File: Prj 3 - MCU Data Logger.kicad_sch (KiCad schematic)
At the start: 25 parts, among them U1 24LC1025, U2 24LC1025, U3 DS1337S_, U4 ATMEGA328P-AU, Y1 Crystal, Y2 Crystal

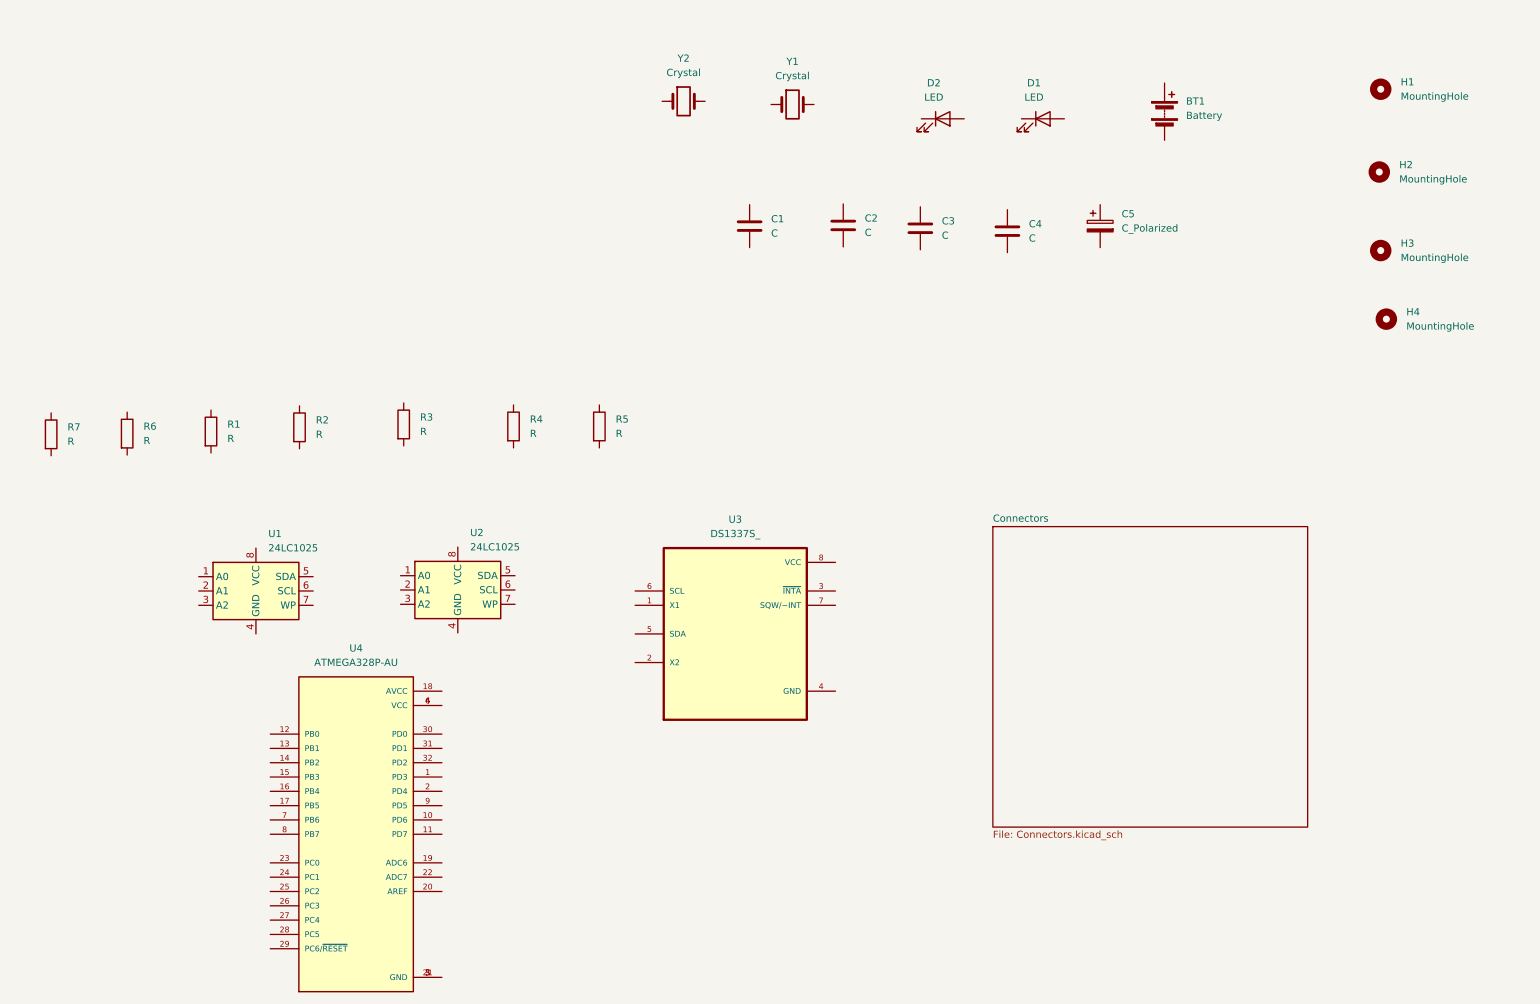
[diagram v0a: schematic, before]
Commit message: Placed symbols and added component values
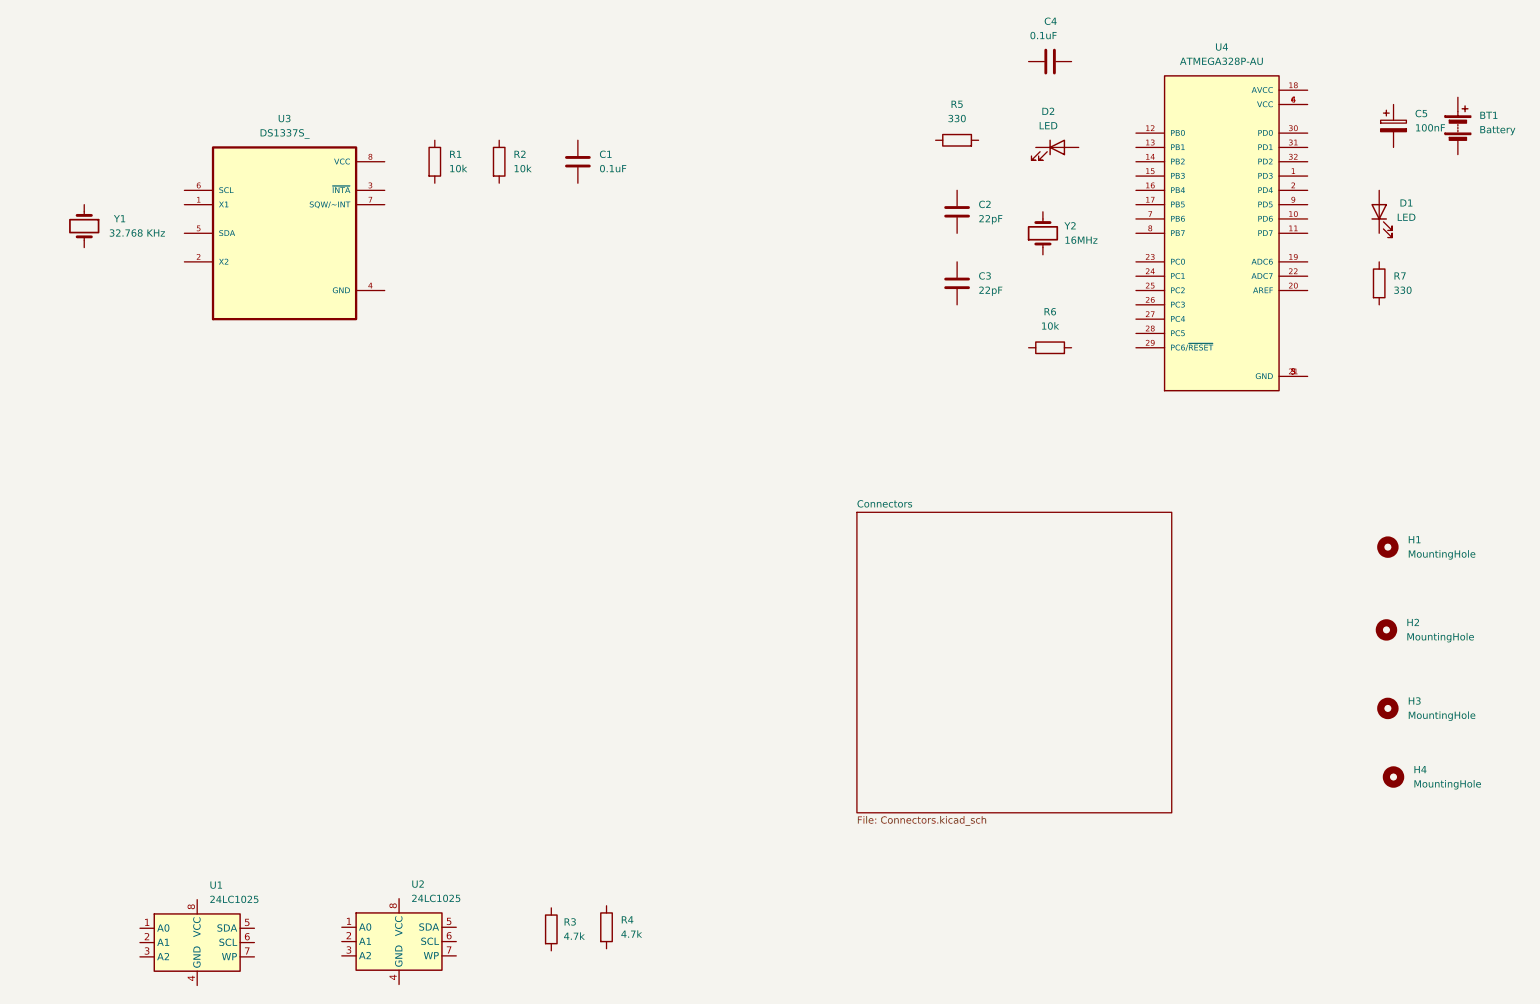
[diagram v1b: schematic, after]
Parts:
- C1, C4: value C -> 0.1uF
- C2: renamed from C3; value C -> 22pF
- C3: renamed from C2; value C -> 22pF
- C5: value C_Polarized -> 100nF
- R1: renamed from R2; value R -> 10k
- R2: renamed from R3; value R -> 10k
- R3: renamed from R6; value R -> 4.7k
- R4: renamed from R1; value R -> 4.7k
- R5: renamed from R4; value R -> 330
- R6: renamed from R7; value R -> 10k
- R7: renamed from R5; value R -> 330
- Y1: renamed from Y2; value Crystal -> 32.768 KHz
- Y2: renamed from Y1; value Crystal -> 16MHz
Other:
- moved on the sheet: BT1, C1, C2, C3, C4, C5, D1, D2, H1, H2, H3, H4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

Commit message: add footprints to symbols
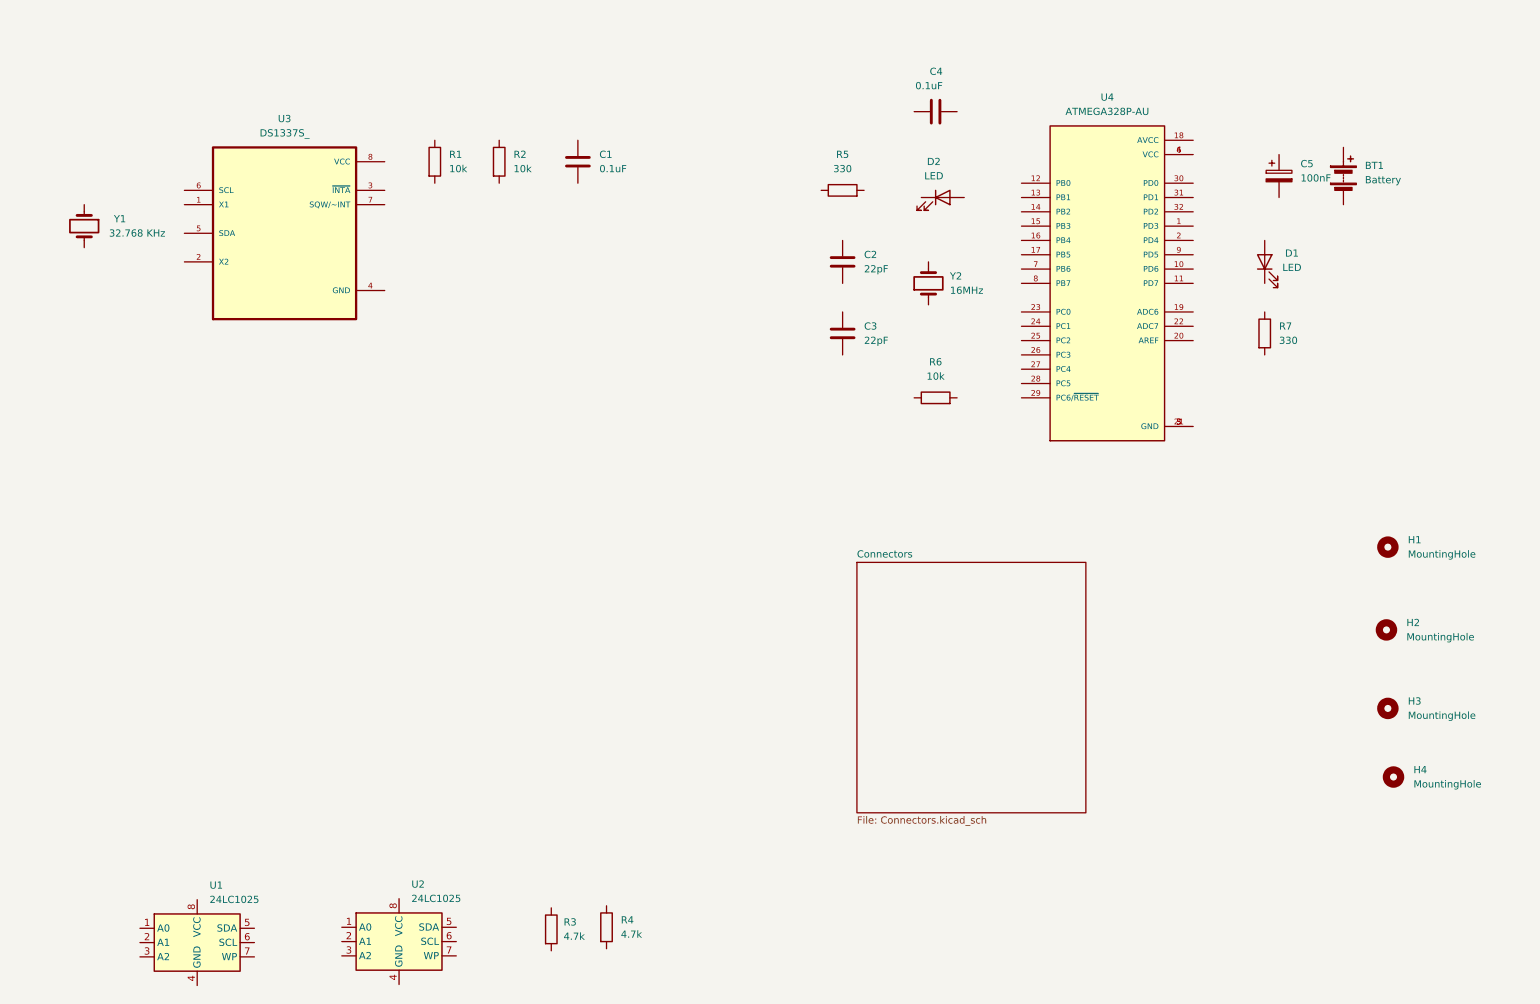
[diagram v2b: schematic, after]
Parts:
- BT1: footprint (none) -> Connector_PinHeader_2.54mm:PinHeader_1x02_P2.54mm_Vertical
- C1, C2, C3, C4, C5: footprint (none) -> Capacitor_SMD:C_0805_2012Metric
- D1, D2: footprint (none) -> LED_SMD:LED_0805_2012Metric
- H1, H2, H3, H4: footprint (none) -> MountingHole:MountingHole_2.1mm
- R1, R2, R3, R4, R5, R6, R7: footprint (none) -> Resistor_SMD:R_0805_2012Metric
- U1, U2: footprint (none) -> Package_SO:SOIC-8_5.23x5.23mm_P1.27mm
- U3: footprint DS1337S_:SOIC127P600X175-8N -> DS1337S:DS1337S
- U4: footprint ATMEGA328P-AU:QFP80P900X900X120-32N -> ATMEGA328P-AU:ATMEGA328P-AU
- Y1, Y2: footprint (none) -> Crystal:Crystal_SMD_5032-2Pin_5.0x3.2mm_HandSoldering
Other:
- moved on the sheet: BT1, C2, C3, C4, C5, D1, D2, R5, R6, R7, U4, Y2

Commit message: Wiring completed
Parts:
- renumbered D2 to D1, D1 to D2
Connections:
- net Vcc: now reaches U1.1 (A0)
- net Vcc: now also C1.1, R1.1, R2.1, R3.1, R4.1, R6.1, U1.2 (A1), U1.3 (A2), U1.8 (VCC), U2.1 (A0), U2.3 (A2), U2.8 (VCC), U3.8 (VCC)
- net GND: now reaches U1.4 (GND)
- net GND: now also BT1.2 (-), C1.2, C2.1, C3.1, C4.1, C5.2, R5.1, R7.2, U1.7 (WP), U2.2 (A1), U2.4 (GND), U2.7 (WP), U3.4 (GND), U4.21 (GND), U4.3 (GND), U4.5 (GND)
- net SDA: now reaches U1.5 (SDA)
- net SDA: now also R4.2, U2.5 (SDA), U3.5 (SDA), U4.27 (PC4)
- net SCK: now reaches U1.6 (SCL)
- net SCK: now also D1.2 (A), R3.2, U2.6 (SCL), U3.6 (SCL), U4.17 (PB5), U4.28 (PC5)
- net at R5.2: now also D1.1 (K)
- net at R1.2: now also U3.3 (~{INTA})
- net at C2.2: now also U4.7 (PB6), Y2.2
- net at C3.2: now also U4.8 (PB7), Y2.1
- net D3: now reaches U4.1 (PD3)
- net D6: now reaches U4.10 (PD6)
- net D7: now reaches U4.11 (PD7)
- net D8: now reaches U4.12 (PB0)
- net MOSI: now reaches U4.15 (PB3)
- net MISO: now reaches U4.16 (PB4)
- net at U4.18 (AVCC): now also BT1.1 (+), C5.1, D2.2 (A), U4.4 (VCC)
- net D4: now reaches U4.2 (PD4)
- net at U4.20 (AREF): now also C4.2
- net RESET: now reaches U4.29 (PC6/~{RESET})
- net RESET: now also R6.2
- net RX: now reaches U4.30 (PD0)
- net TX: now reaches U4.31 (PD1)
- net D2: now reaches U4.32 (PD2)
- net at U4.6 (VCC): no longer U4.4 (VCC)
- net D5: now reaches U4.9 (PD5)
- net at Y1.1: now also U3.1 (X1)
- net at Y1.2: now also U3.2 (X2)
- net at U3.7 (SQW/~INT): now also R2.2
- net at D2.1 (K): now also R7.1
- no-connect marks 0 -> 9
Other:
- sheet Connectors ports: added D2, D3, D4, D5, D6, D7, D8, GND, MISO, MOSI, RESET, RX, SCK, SDA, TX, Vcc; removed none
- moved on the sheet: BT1, C2, C3, C4, C5, D1, R3, R4, R5, U1, U2, Y1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

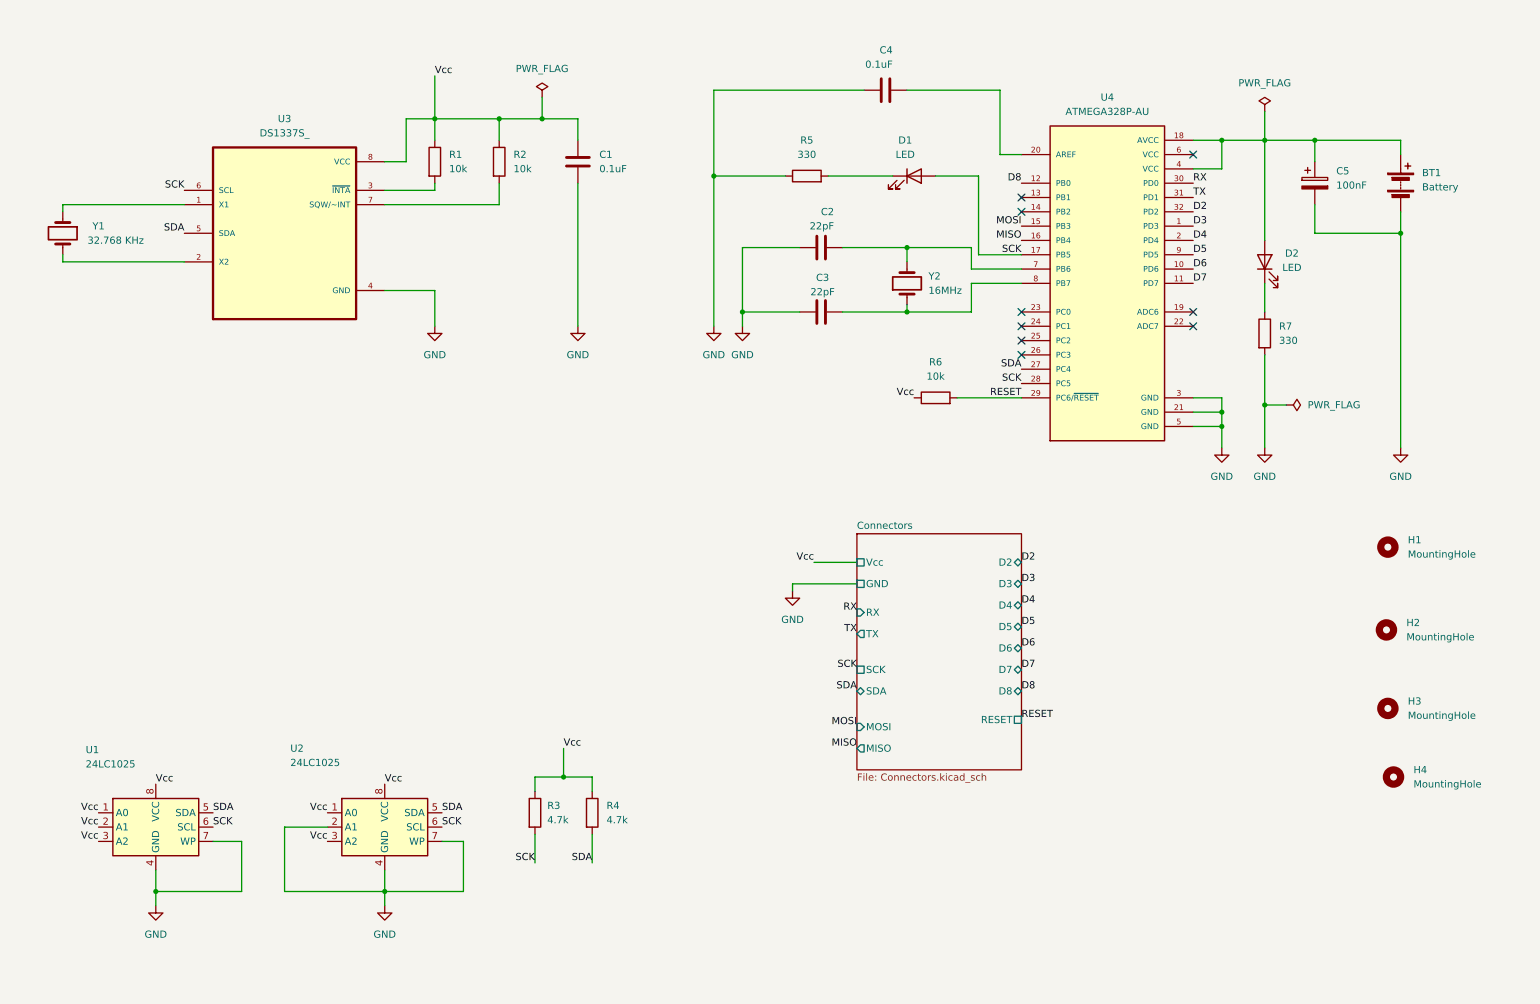
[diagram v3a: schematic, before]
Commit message: schematic completed
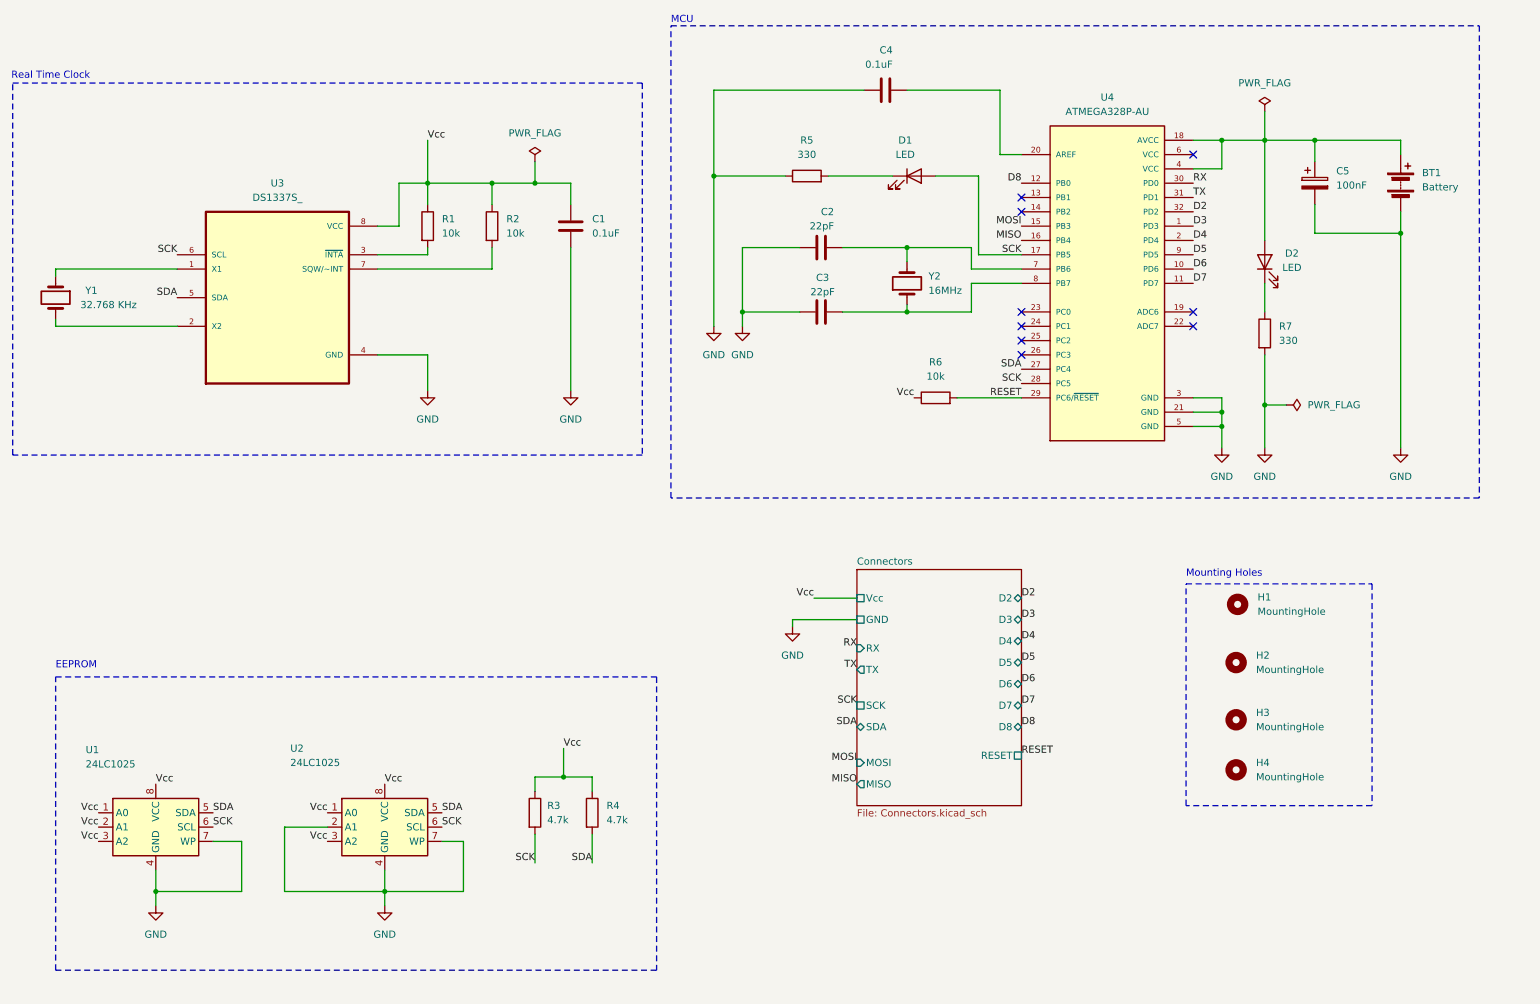
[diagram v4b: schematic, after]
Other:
- note added: "EEPROM"
- note added: "MCU"
- note added: "Mounting Holes"
- note added: "Real Time Clock"
- moved on the sheet: C1, H1, H2, H3, H4, R1, R2, U3, Y1

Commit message: Fixed outstanding issues
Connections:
- net Vcc: now also BT1.1 (+), C5.1, D2.2 (A), U4.18 (AVCC), U4.4 (VCC)
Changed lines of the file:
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@@
+		)
+	)
+	(label "Vcc"
+		(at 232.41 38.1 0)
+		(fields_autoplaced yes)
+		(effects
+			(font
+				(size 1.27 1.27)
+			)
+			(justify left bottom)
 		)
 	)
